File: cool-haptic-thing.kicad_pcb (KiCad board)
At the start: 2 copper layers, 33.1 x 36.8 mm, 7 parts, among them M1 Motor_DC, Q1 2N3904

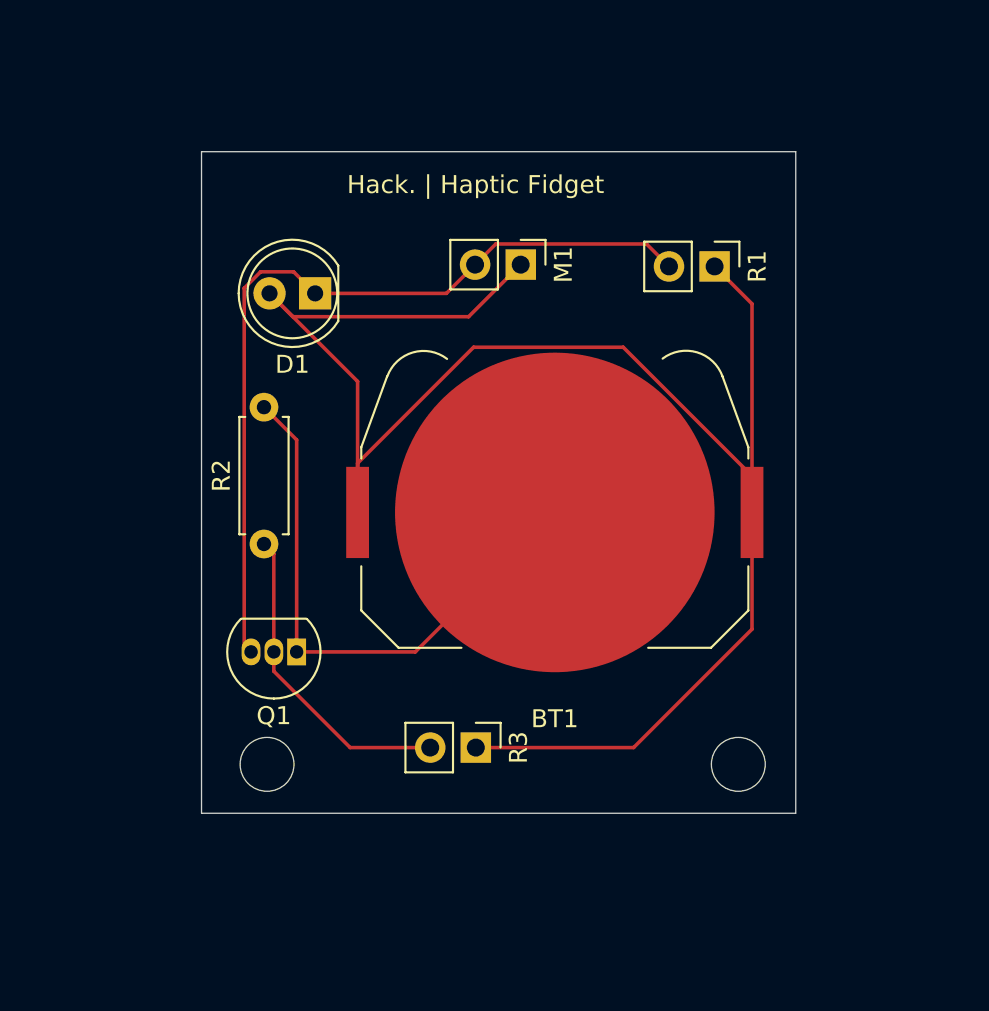
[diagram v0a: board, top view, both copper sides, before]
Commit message: Update
ty cyao for the feedback
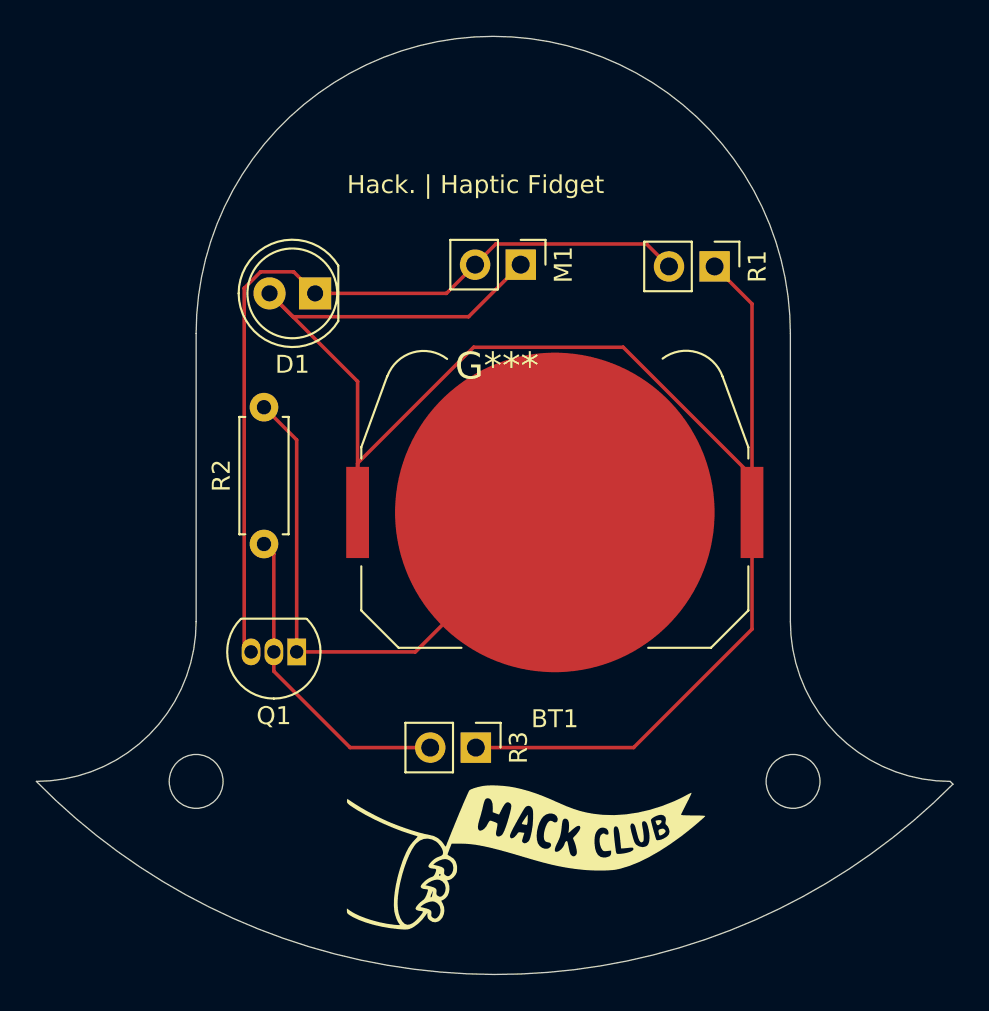
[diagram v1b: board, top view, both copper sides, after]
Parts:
- added G***: LOGO, LOGO, F.Cu at (74.6, 79.4)
- added G***: LOGO, LOGO, B.Cu at (73.0, 52.1)
- added G***: LOGO, LOGO, B.Cu at (72.7, 78.2)
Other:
- board size 33.1 x 36.8 mm -> 51.1 x 52.3 mm
- board text added: "HACK."
